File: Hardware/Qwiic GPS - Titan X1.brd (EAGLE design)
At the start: 30.5 x 25.4 mm, 34 parts, among them J1 U.FL, J2 SMD, J3 PTH, J4 SMD, U1 TITAN X1 GPS

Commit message: Added SparkX models to Sparkfun Library
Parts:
- B1: value COIN CELL -> 6.8MM_COIN_CELL; device SparkX:6.8MM_COIN_CELL -> SparkFun-Batteries:BATTCON-6.8MM
- J1: device SparkX:U.FL -> SparkFun-Connectors:U.FL
- J2, J4: value SMD -> Qwiic Right Angle; device SparkX:1X04_1MM_RA -> SparkFun-Connectors:1X04_1MM_RA
- U1: value TITAN X1 GPS -> Titan X1 GPS; device SparkX:TITAN_X1_GPS -> SparkFun-GPS:TITAN_X1_GPS
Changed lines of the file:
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@@
 <element name="JP2" library="SparkFun" package="MICRO-FIDUCIAL" value="FIDUCIALUFIDUCIAL" x="26.67" y="7.62"/>
 <element name="JP6" library="SparkFun" package="MICRO-FIDUCIAL" value="FIDUCIALUFIDUCIAL" x="-1.27" y="24.13"/>
-<element name="J2" library="SparkX" package="1X04_1MM_RA" value="SMD" x="2.54" y="12.7" smashed="yes" rot="R270">
+<element name="J2" library="SparkFun-Connectors" package="1X04_1MM_RA" value="Qwiic Right Angle" x="2.54" y="12.7" smashed="yes" rot="R270">
 <attribute name="NAME" x="0.381" y="14.097" size="0.6096" layer="25" font="vector" ratio="20" rot="R270"/>
+<attribute name="PROD_ID" value="CONN-13729" x="2.54" y="12.7" size="1.778" layer="27" rot="R270" display="off"/>
+<attribute name="VALUE" value="Qwiic Right Angle" x="2.54" y="12.7" size="1.778" layer="27" rot="R270" display="off"/>
 </element>
 <element name="J3" library="SparkX" package="1X04_NO_SILK" value="PTH" x="7.62" y="1.27" smashed="yes">
@@
 </element>
 <element name="FRAME1" library="SparkFun-Aesthetics" package="CREATIVE_COMMONS" value="FRAME-LETTER" x="-20.32" y="-17.78"/>
-<element name="J4" library="SparkX" package="1X04_1MM_RA" value="SMD" x="22.86" y="12.7" smashed="yes" rot="R90">
+<element name="J4" library="SparkFun-Connectors" package="1X04_1MM_RA" value="Qwiic Right Angle" x="22.86" y="12.7" smashed="yes" rot="R90">
 <attribute name="NAME" x="25.019" y="11.303" size="0.6096" layer="25" font="vector" ratio="20" rot="R90"/>
+<attribute name="PROD_ID" value="CONN-13729" x="22.86" y="12.7" size="1.778" layer="27" rot="R90" display="off"/>
+<attribute name="VALUE" value="Qwiic Right Angle" x="22.86" y="12.7" size="1.778" layer="27" rot="R90" display="off"/>
 </element>
 <element name="LOGO1" library="SparkFun-Aesthetics" package="OSHW-LOGO-MINI" value="OSHW-LOGOMINI" x="0" y="2.54" rot="MR0"/>
@@
 <attribute name="VALUE" x="19.812" y="5.207" size="0.6096" layer="27" font="vector" ratio="20" rot="R270" align="top-center"/>
 </element>
-<element name="B1" library="SparkX" package="6.8MM_COIN_CELL" value="COIN CELL" x="24.13" y="3.81" smashed="yes" rot="R135">
+<element name="B1" library="SparkFun-Batteries" package="BATTCON-6.8MM" value="6.8MM_COIN_CELL" x="24.13" y="3.81" smashed="yes" rot="R135">
 <attribute name="NAME" x="24.5790125" y="1.564934375" size="0.762" layer="25" ratio="15" rot="R135"/>
-<attribute name="VALUE" x="26.416" y="1.905" size="0.762" layer="27" ratio="15" rot="R135"/>
+<attribute name="VALUE" value="6.8MM_COIN_CELL" x="26.416" y="1.905" size="0.762" layer="27" ratio="15" rot="R135"/>
+<attribute name="PROD_ID" value="BATT-13734" x="24.13" y="3.81" size="1.778" layer="27" rot="R135" display="off"/>
 </element>
-<element name="U1" library="SparkX" package="TITAN_X1_GPS" value="TITAN X1 GPS" x="12.7" y="12.7" smashed="yes">
+<element name="U1" library="SparkFun-GPS" package="TITAN_X1_GPS" value="Titan X1 GPS" x="12.7" y="12.7" smashed="yes">
 <attribute name="NAME" x="10.16" y="13.97" size="0.762" layer="25" ratio="15"/>
-<attribute name="VALUE" x="8.382" y="7.874" size="0.762" layer="27" ratio="15"/>
+<attribute name="VALUE" value="Titan X1 GPS" x="8.382" y="7.874" size="0.762" layer="27" ratio="15"/>
+<attribute name="PROD_ID" value="GPS-13693" x="12.7" y="12.7" size="1.778" layer="27" display="off"/>
 </element>
 <element name="R7" library="SparkFun-Resistors" package="0603" value="4.7k" x="0" y="2.54" smashed="yes" rot="R270">
@@
 <attribute name="PROD_ID" value="RES-07869" x="24.13" y="17.78" size="1.778" layer="27" font="vector" ratio="15" rot="R90" display="off"/>
 </element>
-<element name="J1" library="SparkX" package="U.FL" value="U.FL" x="-0.127" y="18.415" smashed="yes">
+<element name="J1" library="SparkFun-Connectors" package="U.FL" value="U.FL" x="-0.127" y="18.415" smashed="yes">
 <attribute name="PROD_ID" value="CONN-09193" x="-0.127" y="18.415" size="1.778" layer="27" font="vector" ratio="15" display="off"/>
 <attribute name="SF_ID" value="WRL-09144" x="-0.127" y="18.415" size="1.778" layer="27" font="vector" ratio="15" display="off"/>

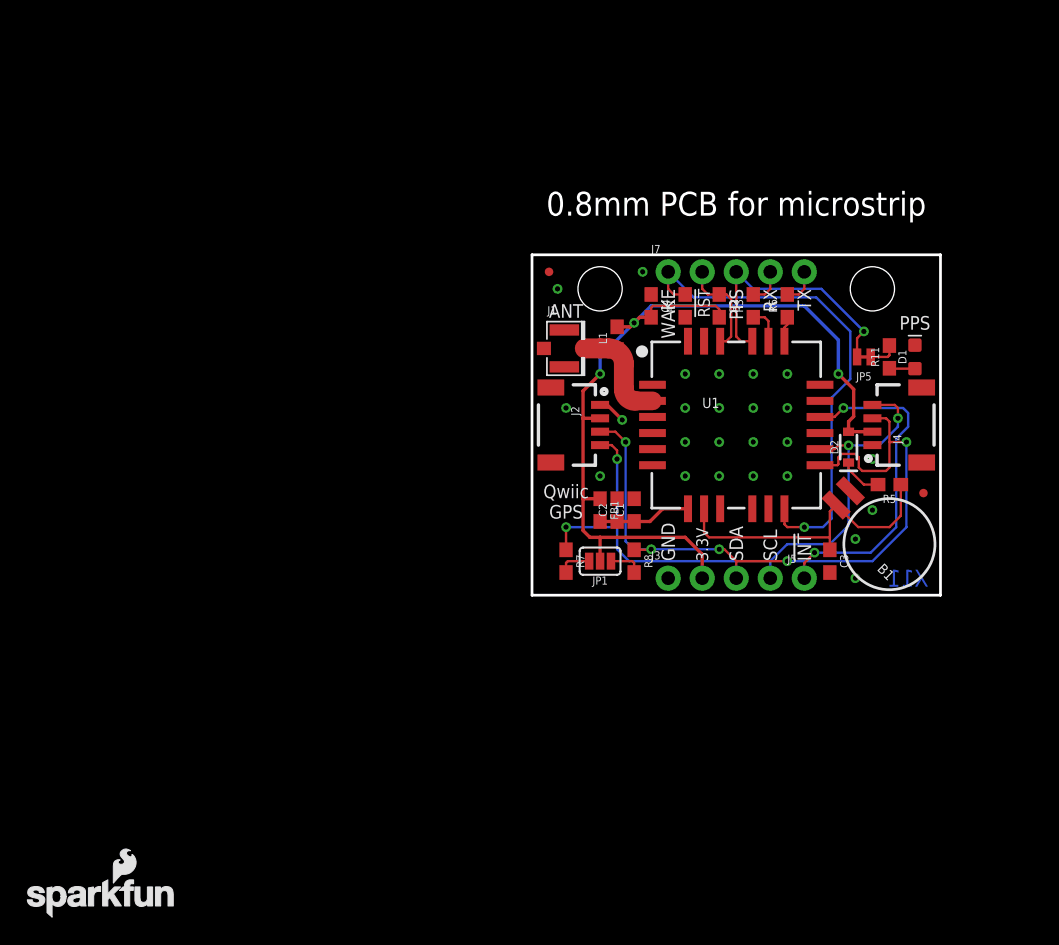
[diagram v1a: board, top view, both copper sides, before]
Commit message: fixed DRC errors, updated board to meet checklist
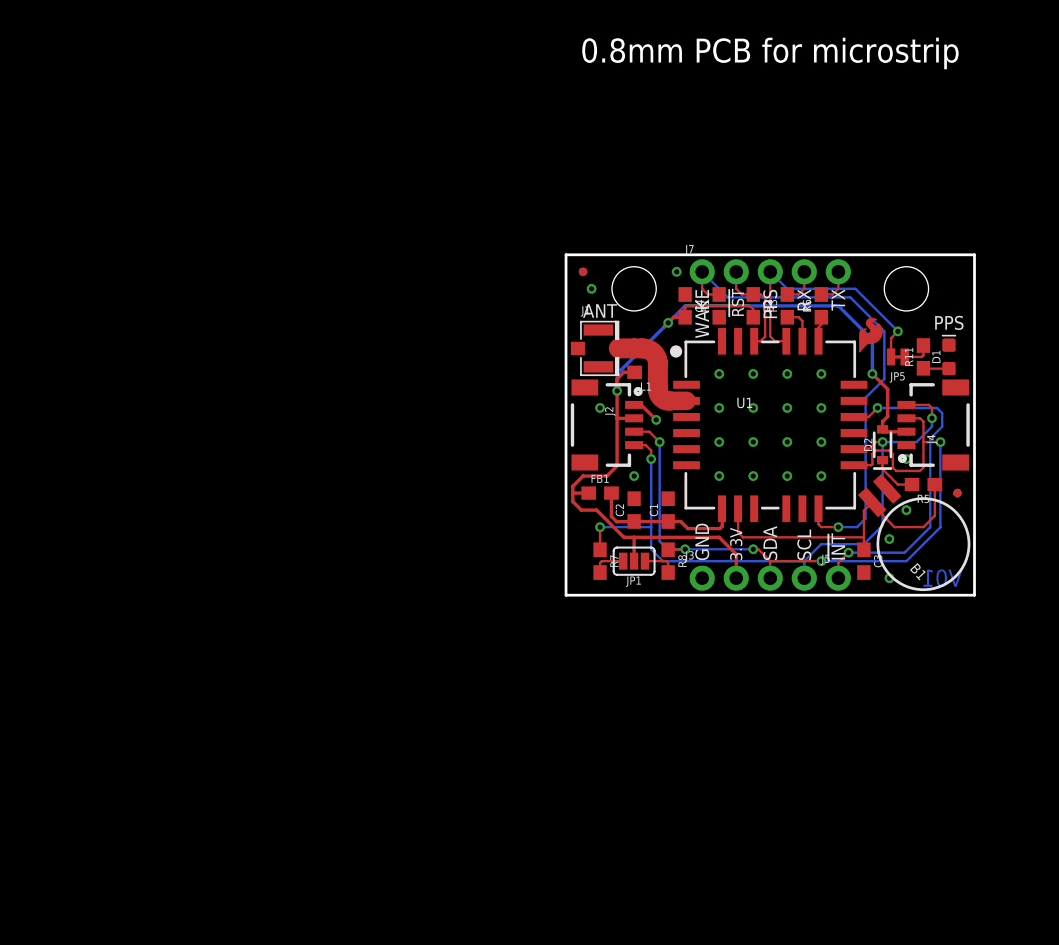
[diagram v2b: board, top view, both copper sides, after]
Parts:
- added JP7, JP8: FIDUCIALUFIDUCIAL, SparkFun:MICRO-FIDUCIAL
- added LOGO3: REVISION, SparkFun-Aesthetics:REVISION
- U$1: device SparkFun-Aesthetics:SFE_LOGO_NAME_.1 -> SparkFun-Aesthetics:SFE_LOGO_FLAME_COPPER_EXPOSED_.1
- moved LOGO2 68.8 mm to (21.2, 6.10), flipped to the bottom
- moved U$1 10.3 mm to (21.6, 17.8), flipped to the top
- moved L1 3.33 mm to (5.97, 16.6), turned to 180 degrees
- moved D2 2.55 mm to (23.6, 11.2)
- moved B1 2.54 mm to (26.7, 3.81), turned to 132 degrees
- moved C3 2.54 mm to (22.2, 2.54)
- moved R11 2.54 mm to (26.7, 17.8)
- moved R5 2.54 mm to (26.7, 8.26)
- moved C4 2.54 mm to (8.89, 21.6)
- moved R2 2.54 mm to (14.0, 21.6)
- moved R3 2.54 mm to (16.5, 21.6)
- moved U1 2.54 mm to (15.2, 12.7)
- moved C1 2.54 mm to (7.62, 6.35)
- moved J1 2.54 mm to (2.41, 18.4)
- moved J2 2.54 mm to (5.08, 12.7)
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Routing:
- net 3.3V: track 68.3 -> 74.1 mm
- net VCC_FILTERED: track 6.95 -> 11.8 mm
- net EXT_ANT: track 9.10 -> 9.97 mm
- net SDA: track 54.1 -> 54.6 mm
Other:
- board text added: "Andrew England"
- board text added: "Measurements in mm"
- board text added: "Nathan Seidle"
- board text added: "V01"
- board text removed: "X11"

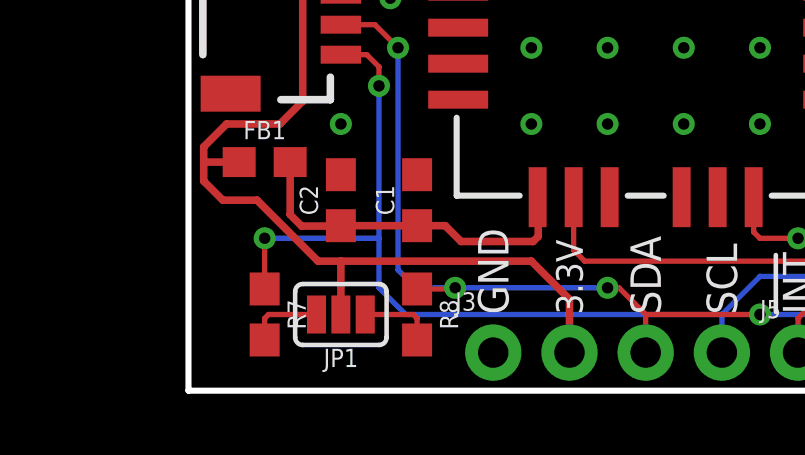
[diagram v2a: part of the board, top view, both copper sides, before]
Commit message: Added jumper functions to schematic and board
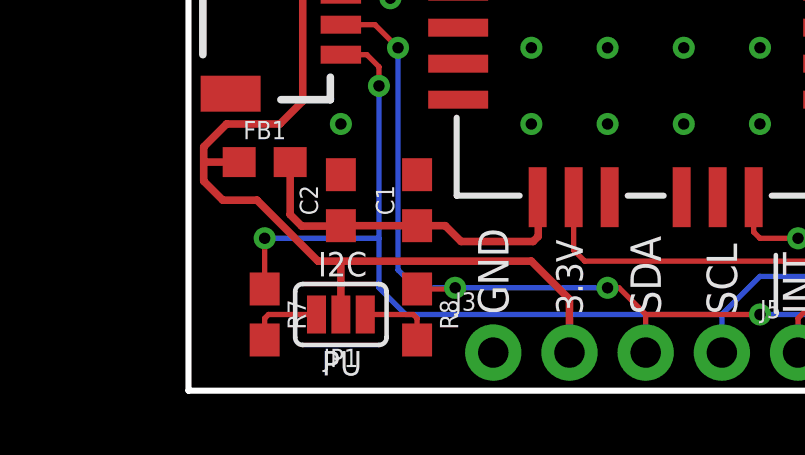
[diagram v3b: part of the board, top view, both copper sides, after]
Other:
- board text added: "I2C"
- board text added: "PU"
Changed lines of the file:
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@@
 <grid distance="0.05" unitdist="inch" unit="inch" style="lines" multiple="1" display="yes" altdistance="0.005" altunitdist="inch" altunit="inch"/>
 <layers>
-<layer number="1" name="Top" color="4" fill="1" visible="no" active="yes"/>
+<layer number="1" name="Top" color="4" fill="1" visible="yes" active="yes"/>
 <layer number="2" name="Route2" color="1" fill="3" visible="no" active="no"/>
 <layer number="3" name="Route3" color="4" fill="3" visible="no" active="no"/>
@@
 <layer number="14" name="Route14" color="1" fill="6" visible="no" active="no"/>
 <layer number="15" name="Route15" color="4" fill="6" visible="no" active="no"/>
-<layer number="16" name="Bottom" color="1" fill="1" visible="no" active="yes"/>
+<layer number="16" name="Bottom" color="1" fill="1" visible="yes" active="yes"/>
 <layer number="17" name="Pads" color="2" fill="1" visible="yes" active="yes"/>
 <layer number="18" name="Vias" color="2" fill="1" visible="yes" active="yes"/>
@@
 <layer number="23" name="tOrigins" color="15" fill="1" visible="yes" active="yes"/>
 <layer number="24" name="bOrigins" color="15" fill="1" visible="no" active="yes"/>
-<layer number="25" name="tNames" color="7" fill="1" visible="no" active="yes"/>
+<layer number="25" name="tNames" color="7" fill="1" visible="yes" active="yes"/>
 <layer number="26" name="bNames" color="7" fill="1" visible="no" active="yes"/>
 <layer number="27" name="tValues" color="7" fill="1" visible="no" active="yes"/>
@@
 <dimension x1="0" y1="0" x2="10.16" y2="0" x3="5.08" y3="-3.81" textsize="1.778" layer="47"/>
 <text x="1.27" y="-8.89" size="1.778" layer="47">Measurements in mm</text>
+<text x="4.318" y="3.81" size="0.8128" layer="21" font="vector">I2C</text>
+<text x="4.445" y="0.508" size="0.8128" layer="21" font="vector">PU</text>
 </plain>
 <attributes>

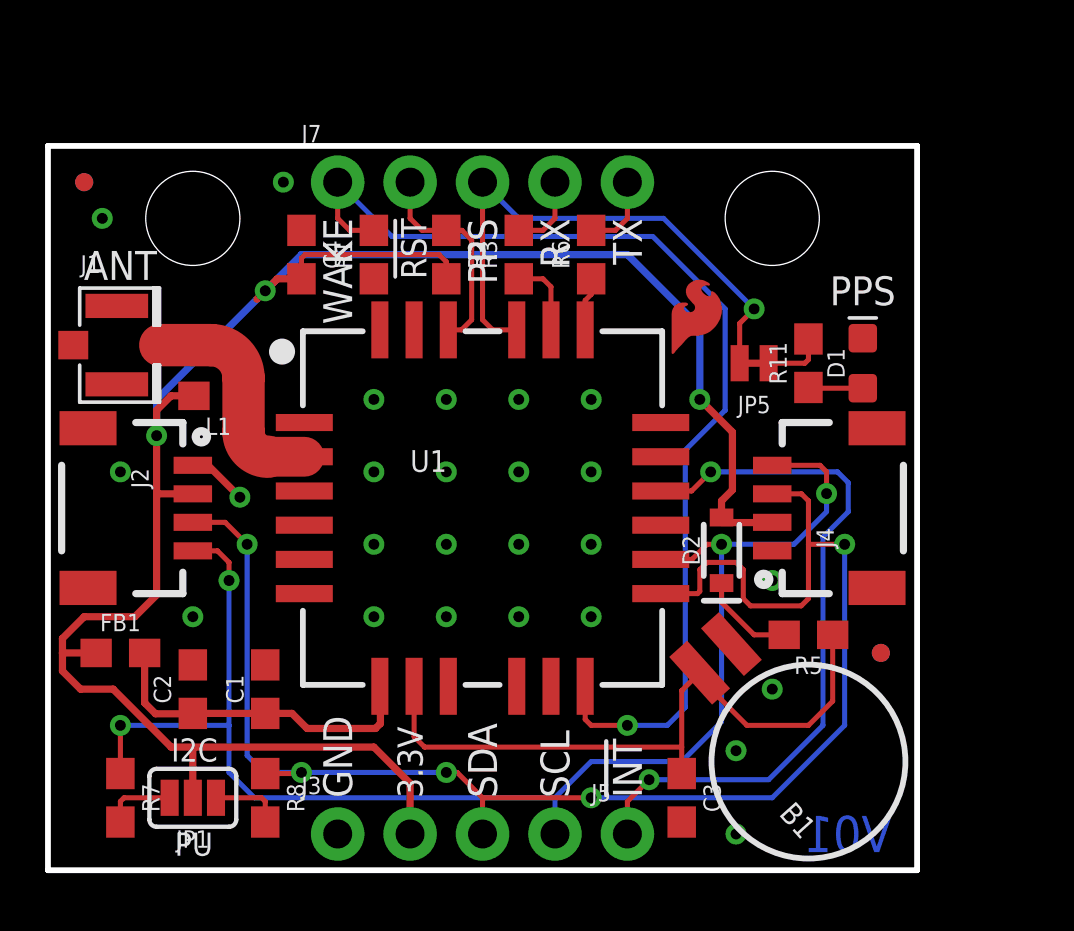
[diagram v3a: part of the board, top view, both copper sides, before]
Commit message: Post design review changes fixed
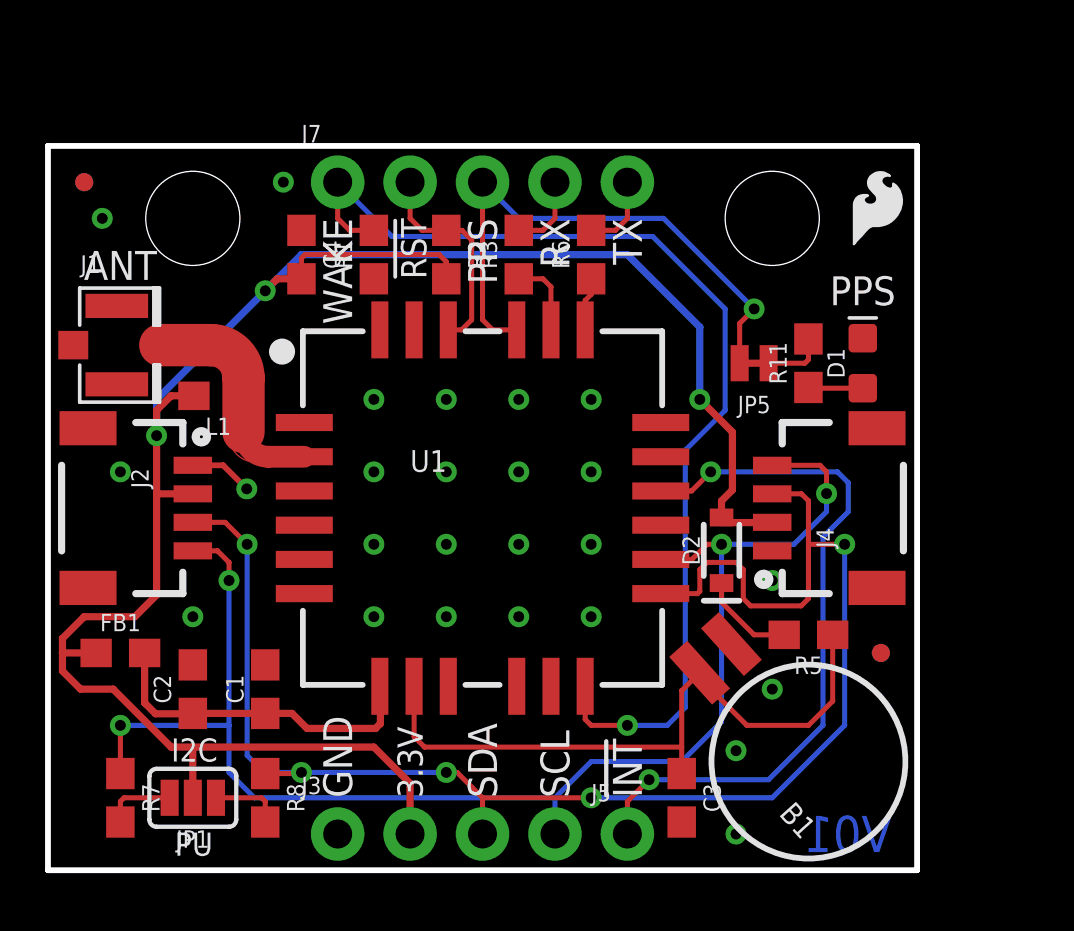
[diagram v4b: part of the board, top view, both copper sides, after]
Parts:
- removed U$1: (no value), SparkFun-Aesthetics:SFE_LOGO_FLAME_COPPER_EXPOSED_.1
- added U$2: (no value), SparkFun-Aesthetics:SFE_LOGO_FLAME_.1
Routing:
- added copper zone on layer 1, net EXT_ANT
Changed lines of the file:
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@@
 <setting verticaltext="up"/>
 </settings>
-<grid distance="0.05" unitdist="inch" unit="inch" style="lines" multiple="1" display="yes" altdistance="0.005" altunitdist="inch" altunit="inch"/>
+<grid distance="0.05" unitdist="inch" unit="inch" style="lines" multiple="1" display="yes" altdistance="0.0005" altunitdist="inch" altunit="inch"/>
 <layers>
 <layer number="1" name="Top" color="4" fill="1" visible="yes" active="yes"/>
@@
 <layer number="17" name="Pads" color="2" fill="1" visible="yes" active="yes"/>
 <layer number="18" name="Vias" color="2" fill="1" visible="yes" active="yes"/>
-<layer number="19" name="Unrouted" color="6" fill="1" visible="no" active="yes"/>
+<layer number="19" name="Unrouted" color="6" fill="1" visible="yes" active="yes"/>
 <layer number="20" name="Dimension" color="15" fill="1" visible="yes" active="yes"/>
 <layer number="21" name="tPlace" color="16" fill="1" visible="yes" active="yes"/>
@@
 <dimension x1="0" y1="0" x2="10.16" y2="0" x3="5.08" y3="-3.81" textsize="1.778" layer="47"/>
 <text x="1.27" y="-8.89" size="1.778" layer="47">Measurements in mm</text>
-<text x="4.318" y="3.81" size="0.8128" layer="21" font="vector">I2C</text>
-<text x="4.445" y="0.508" size="0.8128" layer="21" font="vector">PU</text>
+<text x="4.318" y="3.81" size="0.8128" layer="21" font="vector" ratio="15">I2C</text>
+<text x="4.445" y="0.508" size="0.8128" layer="21" font="vector" ratio="15">PU</text>
 </plain>
 <attributes>
@@
 <element name="JP7" library="SparkFun" package="MICRO-FIDUCIAL" value="FIDUCIALUFIDUCIAL" x="29.21" y="7.62" rot="MR0"/>
 <element name="JP8" library="SparkFun" package="MICRO-FIDUCIAL" value="FIDUCIALUFIDUCIAL" x="1.27" y="24.13" rot="MR0"/>
-<element name="U$1" library="SparkFun-Aesthetics" package="SFE_LOGO_FLAME_COPPER_EXPOSED_.1" value="" x="21.59" y="17.78"/>
+<element name="U$2" library="SparkFun-Aesthetics" package="SFE_LOGO_FLAME_.1" value="" x="27.94" y="21.59"/>
 </elements>
 <signals>
@@
 <wire x1="8.89" y1="21.59" x2="7.62" y2="20.32" width="0.254" layer="16"/>
 <wire x1="3.81" y1="15.24" x2="3.81" y2="16.51" width="0.254" layer="16"/>
-<wire x1="7.62" y1="20.32" x2="7.327" y2="20.027" width="0.254" layer="1"/>
 <wire x1="5.119" y1="16.637" x2="4.318" y2="16.637" width="0.254" layer="1"/>
 <wire x1="4.318" y1="16.637" x2="3.81" y2="16.129" width="0.254" layer="1"/>
@@
 <vertex x="30.48" y="0"/>
 </polygon>
-<polygon width="0.254" layer="1" isolate="0.3048">
+<polygon width="0.254" layer="1" isolate="0.3048" rank="2">
 <vertex x="0" y="0"/>
 <vertex x="0" y="25.4"/>
@@
 <via x="13.97" y="11.43" extent="1-16" drill="0.381"/>
 <via x="13.97" y="8.89" extent="1-16" drill="0.381"/>
-<via x="6.731" y="13.081" extent="1-16" drill="0.381"/>
+<via x="6.9723" y="13.3731" extent="1-16" drill="0.381"/>
 <wire x1="5.08" y1="14.2" x2="5.612" y2="14.2" width="0.254" layer="1"/>
-<wire x1="5.612" y1="14.2" x2="6.731" y2="13.081" width="0.254" layer="1"/>
 <via x="2.54" y="13.97" extent="1-16" drill="0.381"/>
 <via x="1.905" y="22.86" extent="1-16" drill="0.381"/>
@@
 <contactref element="J1" pad="2"/>
 <contactref element="J1" pad="1"/>
+<wire x1="5.612" y1="14.2" x2="6.1454" y2="14.2" width="0.2032" layer="1"/>
+<wire x1="6.1454" y1="14.2" x2="6.9723" y2="13.3731" width="0.2032" layer="1"/>
 </signal>
 <signal name="SCL">
@@
 <contactref element="U1" pad="2"/>
 <contactref element="L1" pad="1"/>
-<wire x1="8.99" y1="14.5" x2="7.725" y2="14.5" width="1.397" layer="1"/>
-<wire x1="7.725" y1="14.5" x2="6.858" y2="15.367" width="1.4859" layer="1" curve="-90"/>
+<wire x1="8.99" y1="14.5" x2="7.725" y2="14.5" width="0.762" layer="1"/>
 <wire x1="5.08" y1="18.415" x2="5.715" y2="18.415" width="1.4859" layer="1"/>
-<wire x1="5.715" y1="18.415" x2="6.858" y2="17.272" width="1.4859" layer="1" curve="-90"/>
 <wire x1="6.858" y1="17.272" x2="6.858" y2="15.367" width="1.4859" layer="1"/>
 <wire x1="5.168" y1="18.327" x2="5.08" y2="18.415" width="0.254" layer="1"/>
@@
 <wire x1="6.819" y1="17.311" x2="6.35" y2="17.78" width="0.635" layer="1"/>
 <wire x1="6.858" y1="17.272" x2="6.35" y2="17.78" width="0.254" layer="1"/>
+<wire x1="5.715" y1="18.415" x2="6.858" y2="17.272" width="1.4859" layer="1" curve="-90"/>
+<polygon width="0.4064" layer="1" orphans="yes">
+<vertex x="6.35" y="15.24" curve="90"/>
+<vertex x="7.2771" y="14.3129"/>
+<vertex x="7.6454" y="14.3129" curve="90"/>
+<vertex x="7.6581" y="14.3256"/>
+<vertex x="7.6581" y="14.6812" curve="-90"/>
+<vertex x="7.4041" y="14.9352"/>
+<vertex x="7.4041" y="15.2273" curve="90"/>
+<vertex x="7.3914" y="15.24"/>
+</polygon>
+<wire x1="7.725" y1="14.5" x2="6.858" y2="15.367" width="0.762" layer="1" curve="-90"/>
 </signal>
 <signal name="N$4">
